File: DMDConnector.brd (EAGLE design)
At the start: 30.5 x 20.3 mm, 7 parts

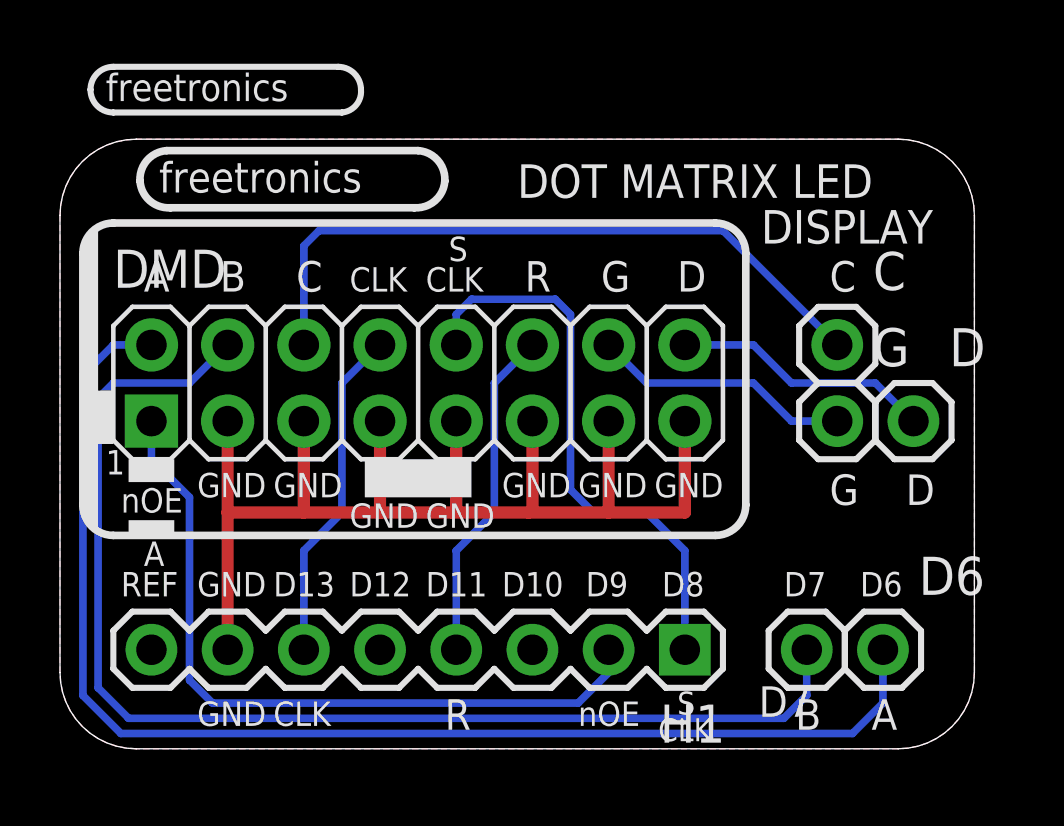
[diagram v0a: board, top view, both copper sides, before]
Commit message: Rename nOE line to OE, add pulldown resistor, bump version to V1.1
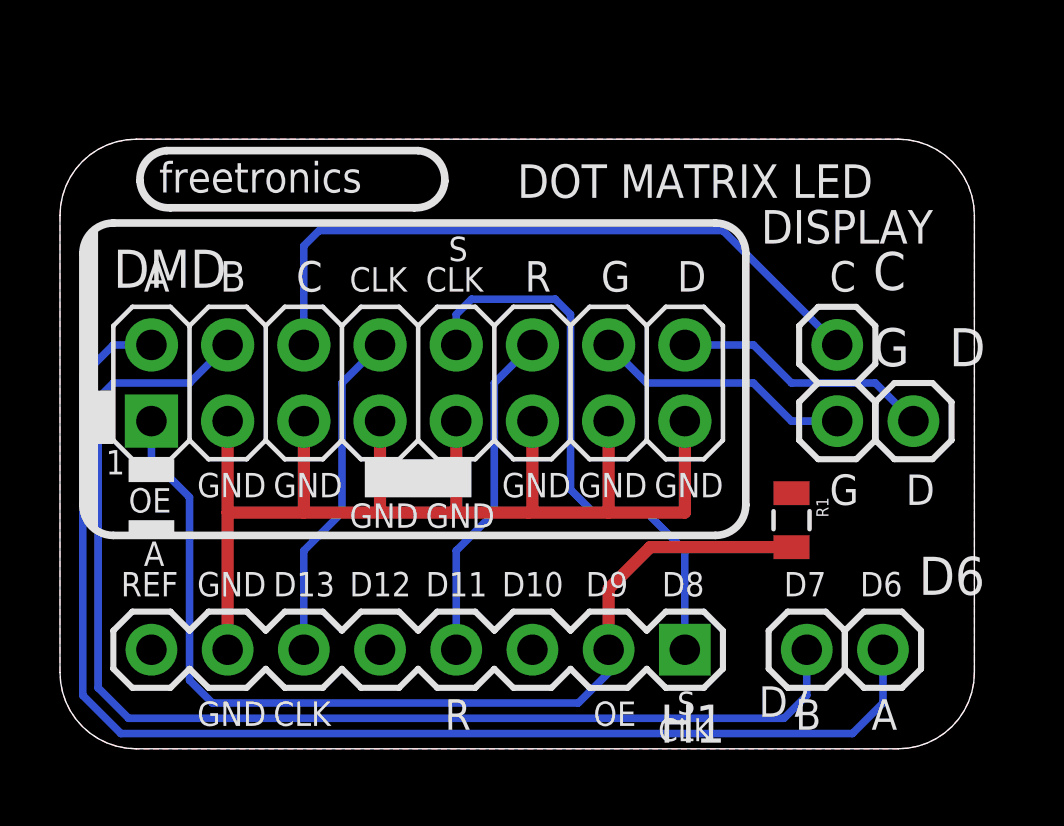
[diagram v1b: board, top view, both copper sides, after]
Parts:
- added R1: 10K, freetronics-master-v1.1:0805
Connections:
- net D9: now also R1.2
- net GND: now also R1.1
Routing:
- net D9: track 24.6 -> 33.3 mm
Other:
- board text added: "(C)2014 Freetronics Pty Ltd"
- board text added: "OE"
- board text added: "SKU: DMDCON V1.1"
- board text removed: "(C)2011 Freetronics Pty Ltd"
- board text removed: "DOT MATRIX"
- board text removed: "LED DISPLAY"
- board text removed: "SKU: DMDCON"
- board text removed: "nOE"
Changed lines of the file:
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@@
 <layers>
 <layer number="1" name="Top" color="4" fill="1" visible="yes" active="yes"/>
+<layer number="2" name="Route2" color="1" fill="3" visible="no" active="no"/>
+<layer number="3" name="Route3" color="4" fill="3" visible="no" active="no"/>
+<layer number="14" name="Route14" color="1" fill="6" visible="no" active="no"/>
+<layer number="15" name="Route15" color="4" fill="6" visible="no" active="no"/>
 <layer number="16" name="Bottom" color="1" fill="1" visible="yes" active="yes"/>
 <layer number="17" name="Pads" color="2" fill="1" visible="yes" active="yes"/>
@@
 <wire x1="1.778" y1="17.526" x2="21.844" y2="17.526" width="0.254" layer="21"/>
 <wire x1="0.762" y1="8.128" x2="0.762" y2="16.51" width="0.254" layer="21"/>
-<wire x1="9.398" y1="21.209" x2="1.778" y2="21.209" width="0.2032" layer="21"/>
-<wire x1="1.778" y1="21.209" x2="1.016" y2="21.971" width="0.2032" layer="21" curve="-90.060185"/>
-<wire x1="1.016" y1="21.971" x2="1.778" y2="22.733" width="0.2032" layer="21" curve="-90.045133"/>
-<wire x1="1.778" y1="22.733" x2="9.271" y2="22.733" width="0.2032" layer="21"/>
-<wire x1="9.271" y1="22.733" x2="10.033" y2="21.971" width="0.2032" layer="21" curve="-90.030084"/>
-<wire x1="10.033" y1="21.971" x2="9.398" y2="21.209" width="0.2032" layer="21" curve="-89.984964"/>
 <wire x1="0.762" y1="16.51" x2="1.778" y2="17.526" width="0.254" layer="21" curve="-90"/>
 <wire x1="21.844" y1="17.526" x2="22.86" y2="16.51" width="0.254" layer="21" curve="-90"/>
@@
 <wire x1="3.683" y1="18.034" x2="2.667" y2="18.923" width="0.254" layer="21" curve="-90.033846"/>
 <wire x1="2.667" y1="18.923" x2="3.556" y2="19.939" width="0.254" layer="21" curve="-89.988722"/>
-<text x="54.102" y="4.445" size="1.016" layer="22" font="vector" ratio="17" rot="MR0">www.freetronics.com/dmd</text>
-<text x="54.102" y="5.715" size="0.8636" layer="22" font="vector" ratio="15" rot="MR0">SKU: DMDCON</text>
+<text x="29.464" y="5.207" size="1.524" layer="22" font="vector" ratio="17" rot="MR0">www.freetronics.com/dmd</text>
+<text x="27.686" y="7.493" size="1.524" layer="22" font="vector" ratio="15" rot="MR0">SKU: DMDCON    V1.1</text>
 <text x="10.668" y="18.288" size="1.016" layer="22" font="vector" ratio="15" rot="MR0">freetronics</text>
-<text x="54.102" y="11.938" size="0.8128" layer="22" font="vector" ratio="17" rot="MR0">(C)2011 Freetronics Pty Ltd</text>
-<text x="53.34" y="8.255" size="0.8636" layer="22" font="vector" ratio="15" rot="MR0">LED DISPLAY</text>
-<text x="53.086" y="9.271" size="0.8636" layer="22" font="vector" ratio="15" rot="MR0">DOT MATRIX</text>
+<text x="21.336" y="15.748" size="0.8128" layer="22" font="vector" ratio="17" rot="MR0">(C)2014 Freetronics Pty Ltd</text>
 <text x="2.032" y="5.08" size="0.8128" layer="21" font="vector" ratio="15">REF</text>
 <text x="4.572" y="5.08" size="0.8128" layer="21" font="vector" ratio="15">GND</text>
@@
 <text x="24.13" y="5.08" size="0.8128" layer="21" font="vector" ratio="15">D7</text>
 <text x="26.67" y="5.08" size="0.8128" layer="21" font="vector" ratio="15">D6</text>
-<text x="2.032" y="7.874" size="0.8128" layer="21" font="vector" ratio="15">nOE</text>
+<text x="2.286" y="7.874" size="0.8128" layer="21" font="vector" ratio="15">OE</text>
 <text x="4.572" y="8.382" size="0.8128" layer="21" font="vector" ratio="15">GND</text>
 <text x="7.112" y="8.382" size="0.8128" layer="21" font="vector" ratio="15">GND</text>
@@
 <text x="7.112" y="0.762" size="0.8128" layer="21" font="vector" ratio="15">CLK</text>
 <text x="12.827" y="0.635" size="1.016" layer="21" font="vector" ratio="17">R</text>
-<text x="17.272" y="0.762" size="0.8128" layer="21" font="vector" ratio="15">nOE</text>
+<text x="17.78" y="0.762" size="0.8128" layer="21" font="vector" ratio="15">OE</text>
 <text x="19.939" y="0.254" size="0.762" layer="21" font="vector" ratio="15">CLK</text>
 <text x="20.574" y="1.143" size="0.762" layer="21" font="vector" ratio="15">S</text>
@@
 <text x="27.051" y="0.635" size="1.016" layer="21" font="vector" ratio="17">A</text>
 <text x="15.24" y="18.3642" size="1.1176" layer="21" font="vector" ratio="18">DOT MATRIX LED</text>
-<text x="1.524" y="21.59" size="0.9144" layer="21" font="vector" ratio="18">freetronics</text>
 <text x="23.368" y="16.8402" size="1.1176" layer="21" font="vector" ratio="18">DISPLAY</text>
 <text x="28.956" y="18.3642" size="1.1176" layer="22" font="vector" ratio="18" rot="MR0">DOT MATRIX LED</text>
@@
 <element name="G" library="freetronics-master-v1" package="1X01" value="M01PTH" x="25.908" y="10.922"/>
 <element name="D" library="freetronics-master-v1" package="1X01" value="M01PTH" x="28.448" y="10.922"/>
+<element name="R1" library="freetronics-master-v1.1" package="0805" value="10K" x="24.384" y="7.62" rot="R270"/>
 </elements>
 <signals>
@@
 <vertex x="0" y="2.54"/>
 </polygon>
+<contactref element="R1" pad="1"/>
 </signal>
 <signal name="AREF">
@@
 <wire x1="4.318" y1="8.382" x2="3.048" y2="9.652" width="0.254" layer="16"/>
 <wire x1="3.048" y1="9.652" x2="3.048" y2="10.922" width="0.254" layer="16"/>
+<contactref element="R1" pad="2"/>
+<wire x1="18.288" y1="3.302" x2="18.288" y2="5.334" width="0.4064" layer="1"/>
+<wire x1="18.288" y1="5.334" x2="19.674" y2="6.72" width="0.4064" layer="1"/>
+<wire x1="19.674" y1="6.72" x2="24.384" y2="6.72" width="0.4064" layer="1"/>
 </signal>
 <signal name="D8">
@@
 </signal>
 </signals>
+<errors>
+</errors>
 </board>
 </drawing>
